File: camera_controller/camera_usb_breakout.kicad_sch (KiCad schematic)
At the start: 19 parts, among them J10 SM08B-NSHSS-TB LFSN, J11 SM06B-NSHSS-TB LFSN, J12 Conn_01x02_Pin, J13 SM04B-NSHSS-TB_LF__SN_, J14 SM03B-NSHSS-TBLFSN, J15 SM03B-NSHSS-TBLFSN, J16 Conn_01x02_Pin, J17 Conn_01x02_Pin, J5 SM03B-NSHSS-TBLFSN, J6 SM03B-NSHSS-TBLFSN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

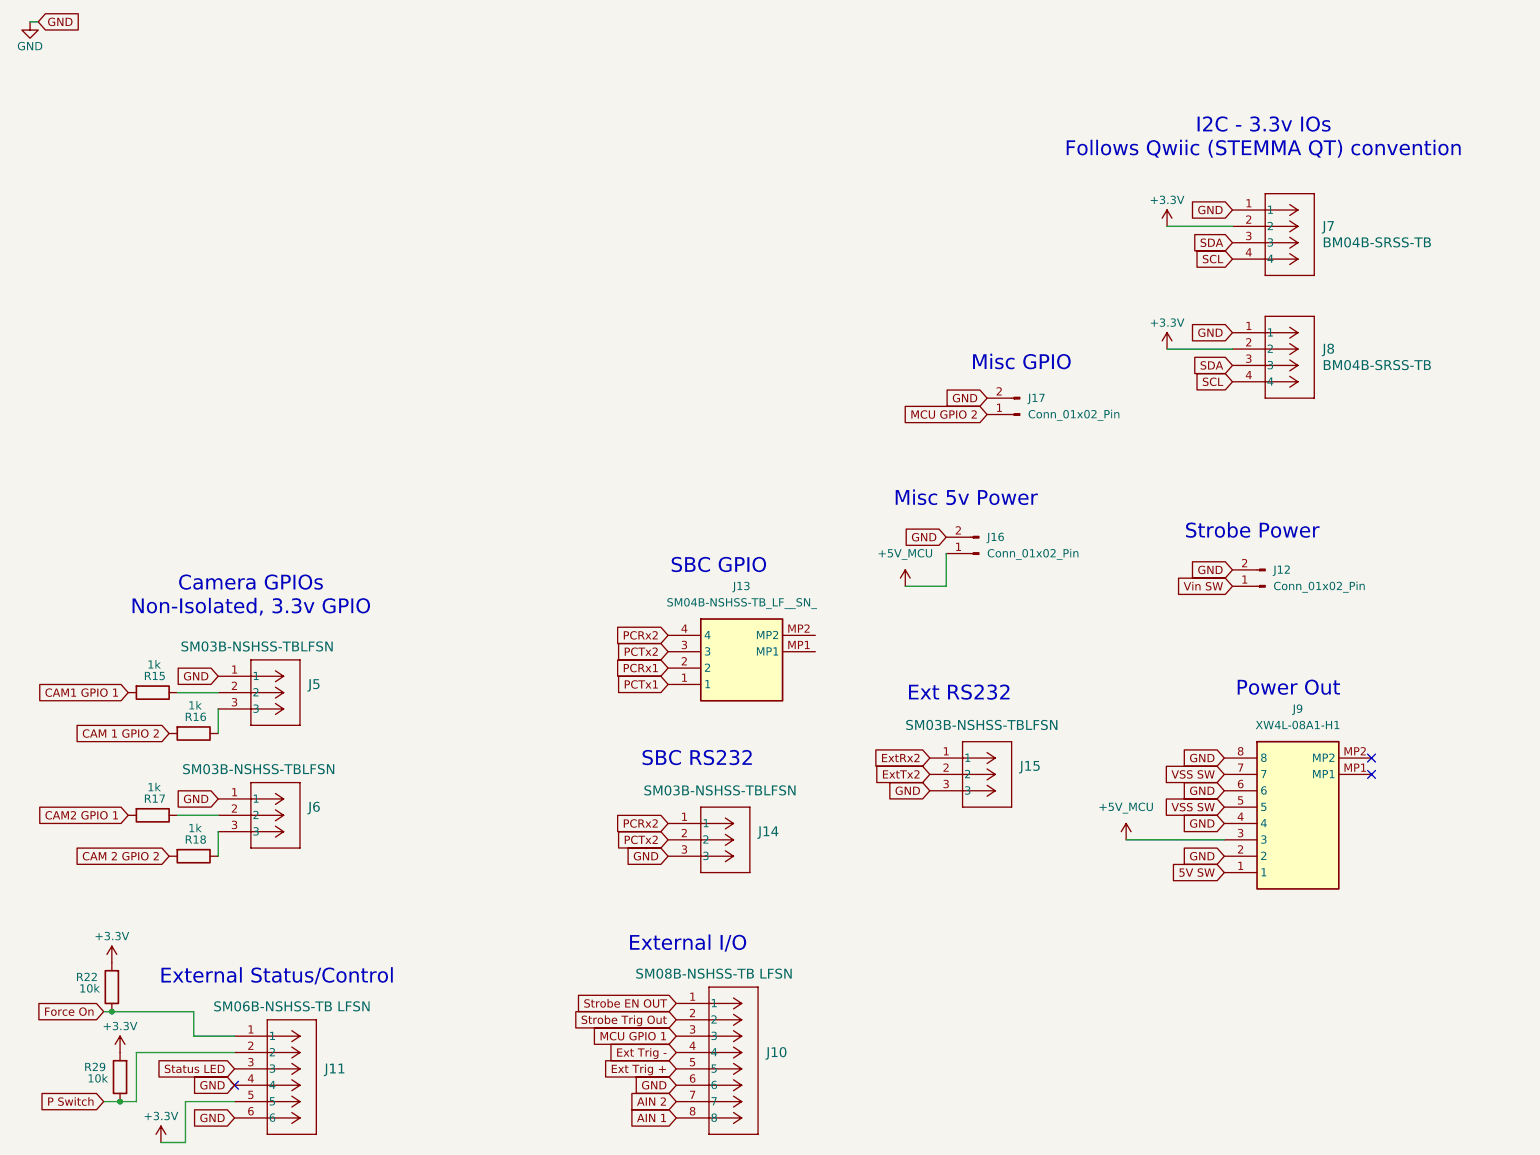
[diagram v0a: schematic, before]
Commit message: Updated connector on controller and added RTO board
Updated the power out connector to a screw clamp design so wires can be released when board is mounted in housing. Added RTO board design.
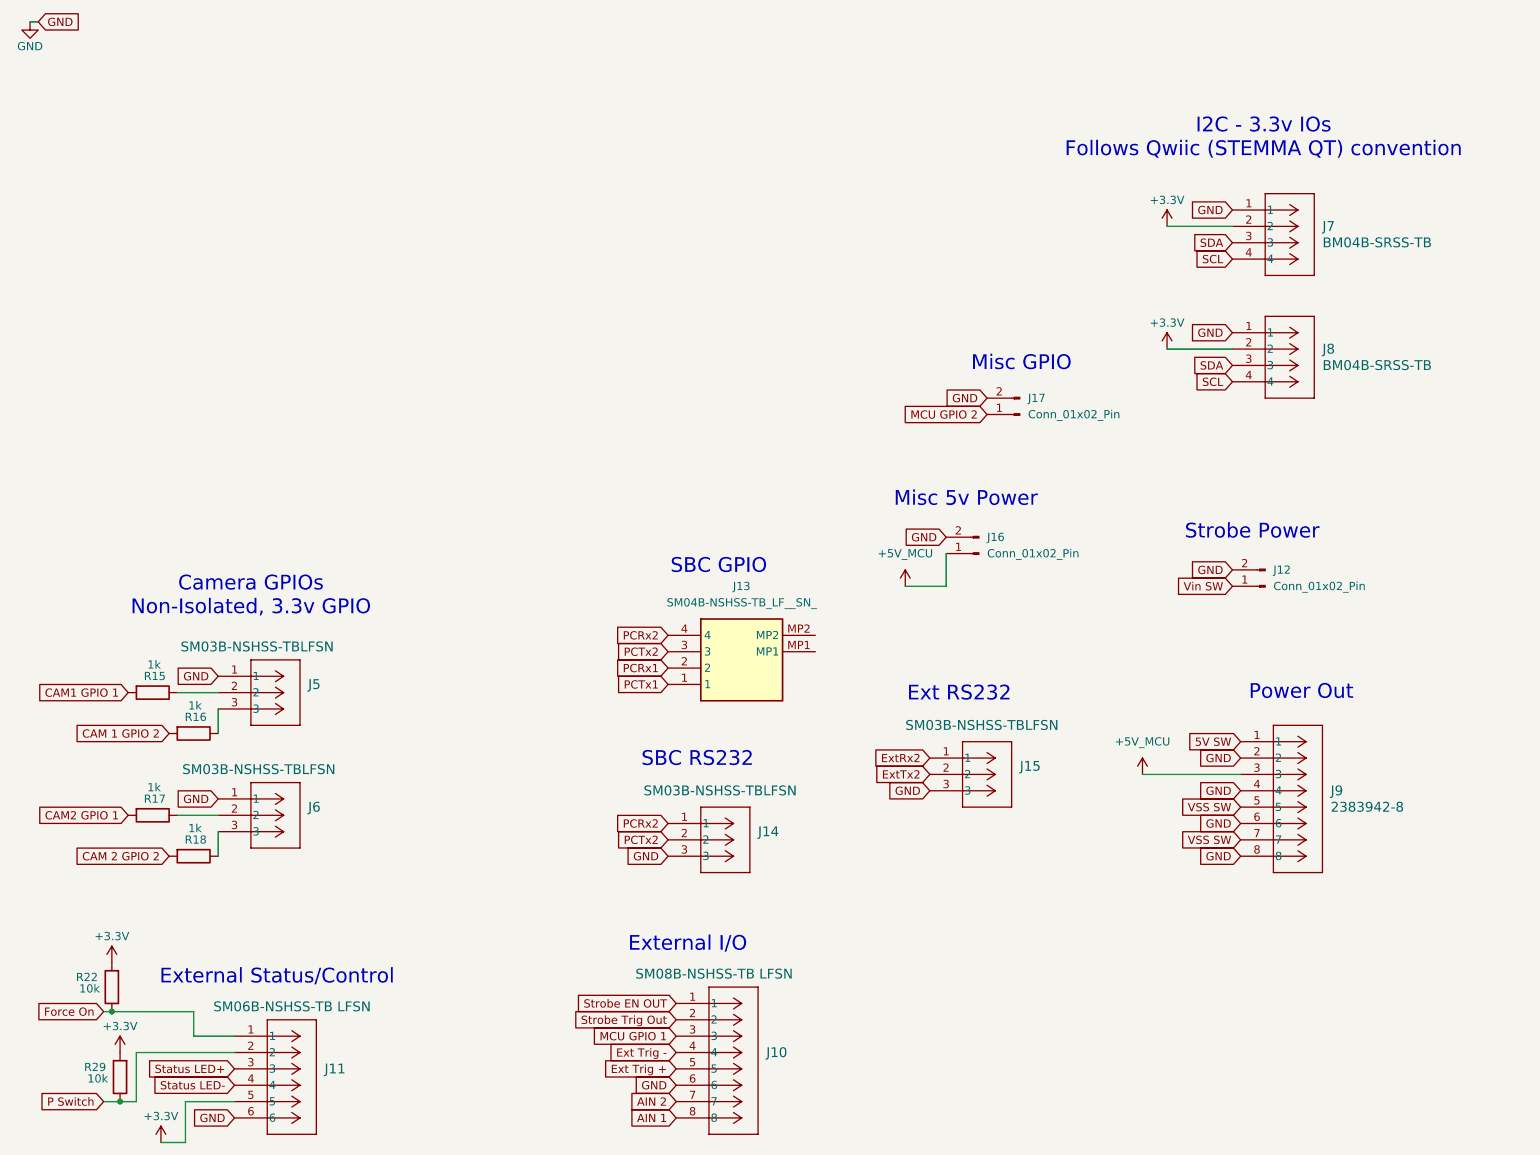
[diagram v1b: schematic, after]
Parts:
- removed J9: XW4L-08A1-H1, Ricks_Library:XW4L08A1H1, symbol Ricks_symbols:XW4L-08A1-H1
- added J9: 2383942-8, Ricks_Library:TERMI-BLOK_SMD_8P_3.5, symbol Ricks_symbols:TERMI-BLOK_SMD_180_8P_3.5
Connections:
- net +5V_MCU: now also J9.3
- net 5V SW: now also J9.1
- net GND: now also J9.2, J9.4, J9.6, J9.8; no longer J11.4
- net VSS SW: now also J9.5, J9.7
- net Status LED renamed Status LED+
- new net Status LED-: J11.4
- no-connect marks 3 -> 0

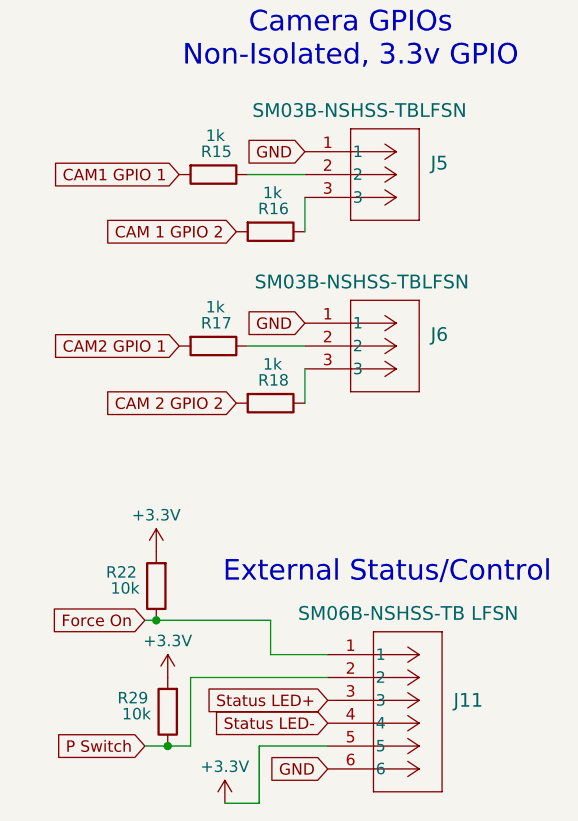
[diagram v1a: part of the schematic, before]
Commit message: Minor updates to controller, 3rd stab at hadron breakout
Minor updates to controller and firmware to make labels more consistent. Took another try at the hadron IO breakout. Old manufacture files removed.
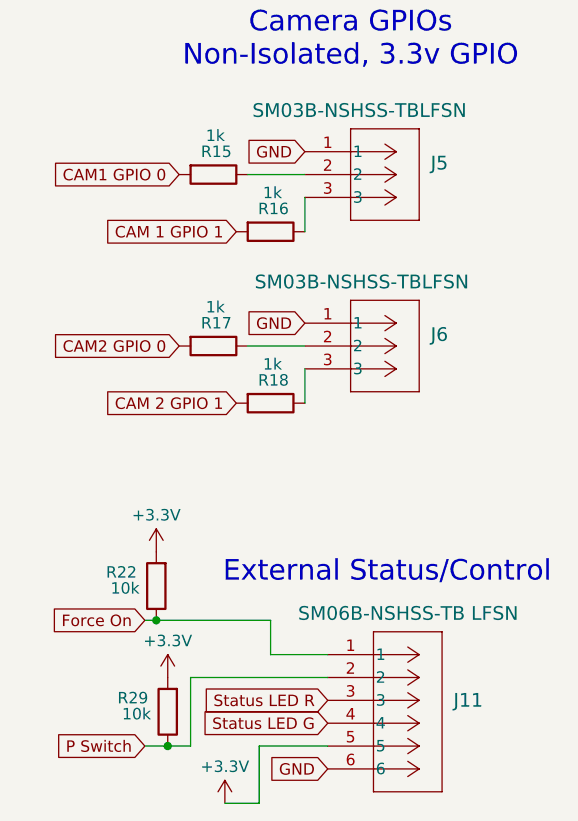
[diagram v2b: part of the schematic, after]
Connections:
- net CAM 1 GPIO 2 renamed CAM 1 GPIO 1
- net CAM 2 GPIO 2 renamed CAM 2 GPIO 1
- net CAM1 GPIO 1 renamed CAM1 GPIO 0
- net CAM2 GPIO 1 renamed CAM2 GPIO 0
- net Status LED+ renamed Status LED R
- net Status LED- renamed Status LED G
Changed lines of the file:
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@@
 		)
 	)
-	(global_label "Status LED-"
+	(global_label "Status LED G"
 		(shape input)
 		(at 53.34 184.15 180)
@@
 		)
 		(property "Intersheetrefs" "${INTERSHEET_REFS}"
-			(at 38.3807 184.15 0)
+			(at 38.3697 184.15 0)
 			(effects
 				(font
@@
 		)
 	)
-	(global_label "CAM2 GPIO 1"
+	(global_label "CAM2 GPIO 0"
 		(shape input)
 		(at 36.83 142.24 180)
@@
 		)
 		(property "Intersheetrefs" "${INTERSHEET_REFS}"
-			(at 21.2053 142.24 0)
+			(at 21.8595 142.24 0)
 			(effects
 				(font
@@
 		)
 	)
-	(global_label "CAM 2 GPIO 2"
+	(global_label "CAM 2 GPIO 1"
 		(shape input)
 		(at 43.18 148.59 180)
@@
 		)
 		(property "Intersheetrefs" "${INTERSHEET_REFS}"
-			(at 26.5877 148.59 0)
+			(at 27.2419 148.59 0)
 			(effects
 				(font
@@
 		)
 	)
-	(global_label "CAM1 GPIO 1"
+	(global_label "CAM1 GPIO 0"
 		(shape input)
 		(at 36.83 123.19 180)
@@
 		)
 		(property "Intersheetrefs" "${INTERSHEET_REFS}"
-			(at 21.2053 123.19 0)
-			(effects
-				(font
-					(size 1.27 1.27)
-				)
-				(justify right)
-				(hide yes)
-			)
-		)
-	)
-	(global_label "Status LED+"
+			(at 21.8595 123.19 0)
+			(effects
+				(font
+					(size 1.27 1.27)
+				)
+				(justify right)
+				(hide yes)
+			)
+		)
+	)
+	(global_label "Status LED R"
 		(shape input)
 		(at 53.34 181.61 180)
@@
 		)
 		(property "Intersheetrefs" "${INTERSHEET_REFS}"
-			(at 38.3807 181.61 0)
+			(at 38.3697 181.61 0)
 			(effects
 				(font
@@
 		)
 	)
-	(global_label "CAM 1 GPIO 2"
+	(global_label "CAM 1 GPIO 1"
 		(shape input)
 		(at 43.18 129.54 180)
@@
 		)
 		(property "Intersheetrefs" "${INTERSHEET_REFS}"
-			(at 26.5877 129.54 0)
-			(effects
-				(font
+			(at 27.2419 129.54 0)
+			(effects
+				(font
